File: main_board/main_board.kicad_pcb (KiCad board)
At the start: 4 copper layers, 45 x 85 mm, 68 parts, among them J1 CON-SMA-EDGE-S, J2 TSW-104-14-F-S, J3 TSW-104-14-F-S, U1 LT1722CS5-TRMPBF, U12 MIC5365-3.3YC5-TR, U2 TS5A4624DCKR, U3 AD5160, U4 TS5A4624DCKR, U5 AD8031ARTZ-REEL7, U6 LT1722CS5-TRMPBF, U7 LTC2315CTS8-12-PBF, U8 LT1818IS5-TRMPBF, U9 AP63205WU-7

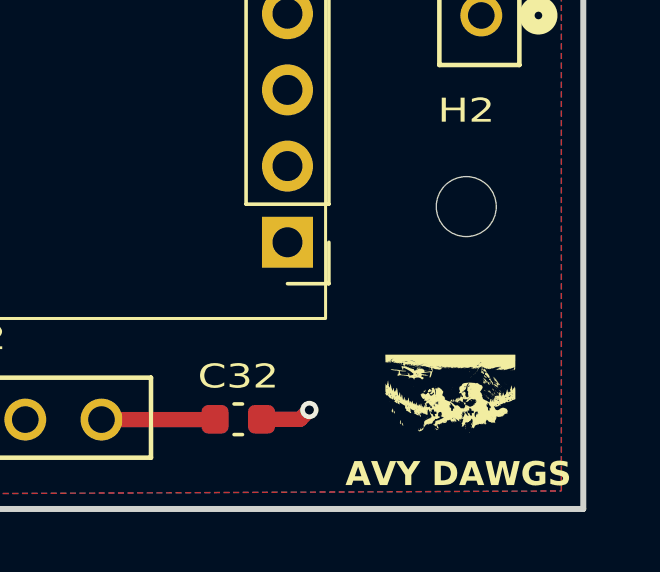
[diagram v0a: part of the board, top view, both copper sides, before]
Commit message: finalized main board, placing order from pcbway.
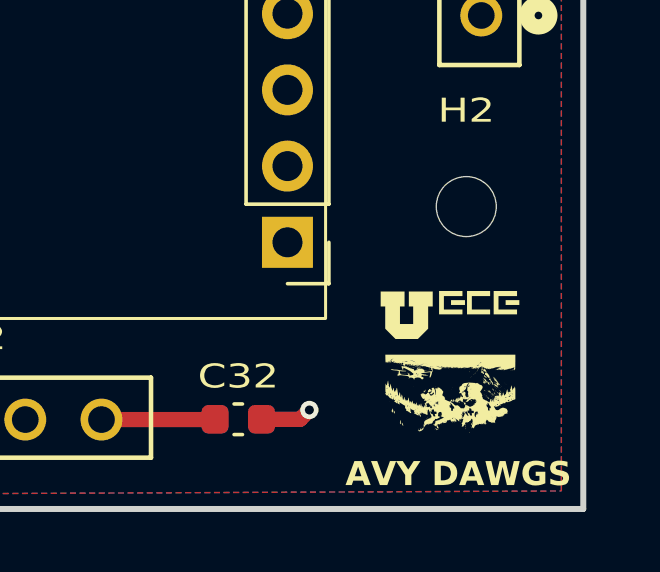
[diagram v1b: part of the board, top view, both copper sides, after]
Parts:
- added G***: LOGO, Graphics:uofu, F.Cu at (158.7, 145.8)
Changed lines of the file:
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@@
 		)
+	)
+	(footprint "Graphics:uofu"
+		(layer "F.Cu")
+		(at 158.7 145.8)
+		(property "Reference" "G***"
+			(at 0.012699 -2.5 0)
+			(layer "F.SilkS")
+			(hide yes)
+			(effects
+				(font
+					(size 1.5 1.5)
+					(thickness 0.3)
+				)
+			)
+		)
+		(property "Value" "LOGO"
+			(at 0.75 0 0)
+			(layer "F.SilkS")
+			(hide yes)
+			(effects
+				(font
+					(size 1.5 1.5)
+					(thickness 0.3)
+				)
+			)
+		)
+		(property "Datasheet" ""
+			(at 0 0 0)
+			(layer "F.Fab")
+			(hide yes)
+			(effects
+				(font
+					(size 1.27 1.27)
+					(thickness 0.15)
+				)
+			)
+		)
+		(property "Description" ""
+			(at 0 0 0)
+			(layer "F.Fab")
+			(hide yes)
+			(effects
+				(font
+					(size 1.27 1.27)
+					(thickness 0.15)
+				)
+			)
+		)
+		(attr board_only exclude_from_pos_files exclude_from_bom)
+		(fp_poly
+			(pts
+				(xy 0.486833 -0.381001) (xy 0.486833 -0.300567) (xy 0.253999 -0.300567) (xy 0.021166 -0.300567)
+				(xy 0.021166 -0.381001) (xy 0.021166 -0.461434) (xy 0.253999 -0.461434) (xy 0.486833 -0.461434)
+			)
+			(stroke
+				(width 0)
+				(type solid)
+			)
+			(fill yes)
+			(layer "F.SilkS")
+		)
+		(fp_poly
+			(pts
+				(xy 2.298699 -0.381001) (xy 2.298699 -0.300567) (xy 2.070099 -0.300567) (xy 1.841499 -0.300567)
+				(xy 1.841499 -0.381001) (xy 1.841499 -0.461434) (xy 2.070099 -0.461434) (xy 2.298699 -0.461434)
+			)
+			(stroke
+				(width 0)
+				(type solid)
+			)
+			(fill yes)
+			(layer "F.SilkS")
+		)
+		(fp_poly
+			(pts
+				(xy 0.402166 -0.681567) (xy 0.402166 -0.596901) (xy 0.093133 -0.596901) (xy -0.215901 -0.596901)
+				(xy -0.215901 -0.372534) (xy -0.215901 -0.148168) (xy 0.093133 -0.148168) (xy 0.402166 -0.148168)
+				(xy 0.402166 -0.067734) (xy 0.402166 0.012699) (xy 0.012699 0.012699) (xy -0.376767 0.012699) (xy -0.376767 -0.376767)
+				(xy -0.376767 -0.766234) (xy 0.012699 -0.766234) (xy 0.402166 -0.766234)
+			)
+			(stroke
+				(width 0)
+				(type solid)
+			)
+			(fill yes)
+			(layer "F.SilkS")
+		)
+		(fp_poly
+			(pts
+				(xy 1.325032 -0.681567) (xy 1.325032 -0.596901) (xy 1.020232 -0.596901) (xy 0.715433 -0.596901)
+				(xy 0.715433 -0.372534) (xy 0.715433 -0.148168) (xy 1.020232 -0.148168) (xy 1.325032 -0.148168)
+				(xy 1.325032 -0.067734) (xy 1.325032 0.012699) (xy 0.939799 0.012699) (xy 0.554566 0.012699) (xy 0.554566 -0.376767)
+				(xy 0.554566 -0.766234) (xy 0.939799 -0.766234) (xy 1.325032 -0.766234)
+			)
+			(stroke
+				(width 0)
+				(type solid)
+			)
+			(fill yes)
+			(layer "F.SilkS")
+		)
+		(fp_poly
+			(pts
+				(xy 2.222499 -0.681567) (xy 2.222499 -0.596901) (xy 1.913466 -0.596901) (xy 1.604432 -0.596901)
+				(xy 1.604432 -0.372534) (xy 1.604432 -0.148168) (xy 1.913466 -0.148168) (xy 2.222499 -0.148168)
+				(xy 2.222499 -0.067734) (xy 2.222499 0.012699) (xy 1.833033 0.012699) (xy 1.443566 0.012699) (xy 1.443566 -0.376767)
+				(xy 1.443566 -0.766234) (xy 1.833033 -0.766234) (xy 2.222499 -0.766234)
+			)
+			(stroke
+				(width 0)
+				(type solid)
+			)
+			(fill yes)
+			(layer "F.SilkS")
+		)
+		(fp_poly
+			(pts
+				(xy -1.528234 -0.499534) (xy -1.528234 -0.249767) (xy -1.604434 -0.249767) (xy -1.680634 -0.249767)
+				(xy -1.680634 0.042333) (xy -1.680634 0.334433) (xy -1.460501 0.334433) (xy -1.240367 0.334433)
+				(xy -1.240367 0.042333) (xy -1.240367 -0.249767) (xy -1.312334 -0.249767) (xy -1.384301 -0.249767)
+				(xy -1.384301 -0.499534) (xy -1.384301 -0.749301) (xy -0.986367 -0.749301) (xy -0.588434 -0.749301)
+				(xy -0.588434 -0.499534) (xy -0.588434 -0.249767) (xy -0.664634 -0.249767) (xy -0.740834 -0.249767)
+				(xy -0.740834 0.120727) (xy -0.740834 0.491221) (xy -0.91236 0.662593) (xy -1.083885 0.833966) (xy -1.456421 0.833966)
+				(xy -1.828956 0.833966) (xy -2.000328 0.66244) (xy -2.171701 0.490915) (xy -2.171701 0.120574) (xy -2.171701 -0.249767)
+				(xy -2.247901 -0.249767) (xy -2.324101 -0.249767) (xy -2.324101 -0.499534) (xy -2.324101 -0.749301)
+				(xy -1.926167 -0.749301) (xy -1.528234 -0.749301)
+			)
+			(stroke
+				(width 0)
+				(type solid)
+			)
+			(fill yes)
+			(layer "F.SilkS")
+		)
+		(embedded_fonts no)
 	)
 	(footprint "LT172x:S_5_ADI"

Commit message: main board gerbers and antenna board layout.
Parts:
- added J4: TSW-104-14-F-S, pin_header_fp:CON4_1X4_TU_TSW, F.Cu at (159.7, 109.7)

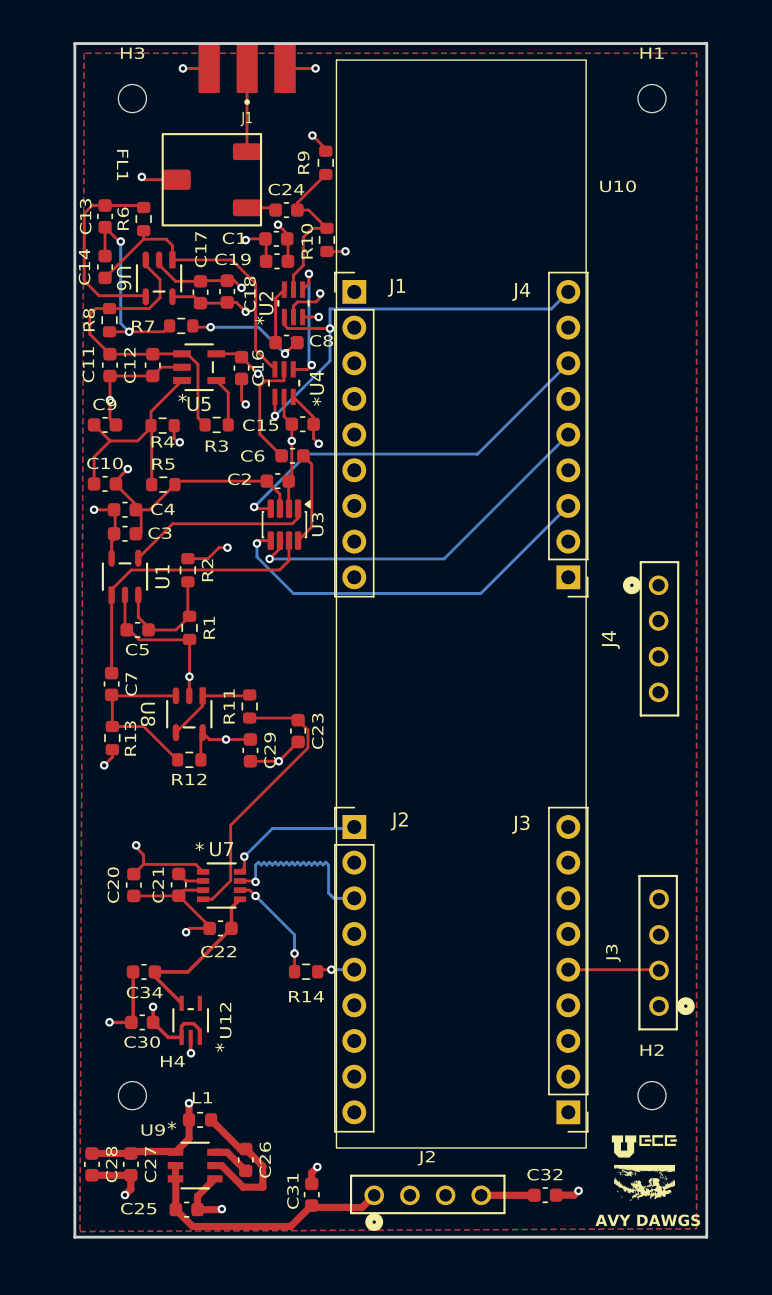
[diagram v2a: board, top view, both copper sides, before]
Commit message: Fixed edge clearance for both boards, both DRC clean
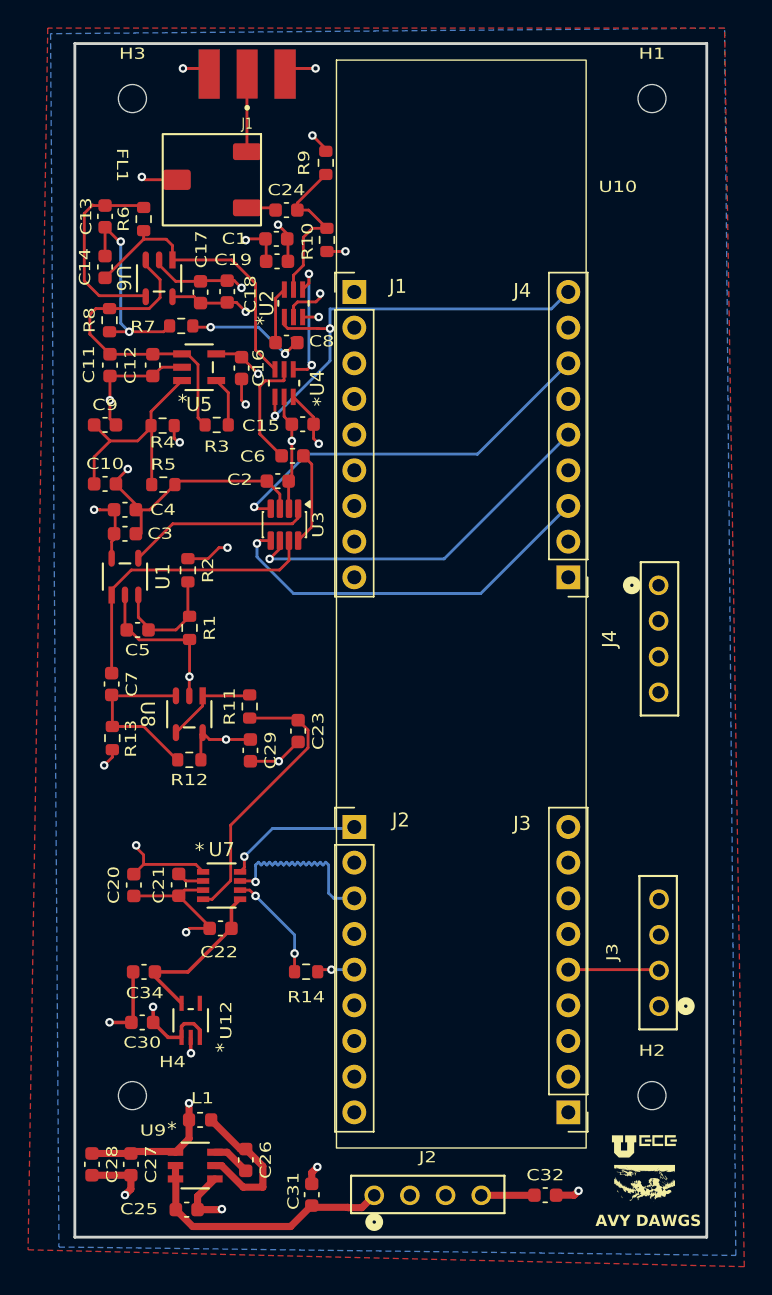
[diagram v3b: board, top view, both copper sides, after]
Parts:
- moved J1 0.40 mm to (130.4, 69.5)
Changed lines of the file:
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@@
 	(footprint "SMA_male_fp:RFSOLUTIONS_CON-SMA-EDGE-S"
 		(layer "F.Cu")
-		(at 130.4 69.0725 -90)
+		(at 130.4 69.4725 -90)
 		(property "Reference" "J1"
-			(at 3.5275 0 180)
+			(at 3.5275 0 0)
 			(layer "F.SilkS")
 			(effects
@@
 		(polygon
 			(pts
-				(xy 118.8 68) (xy 118.5 151.9) (xy 162.4 151.7) (xy 162.4 68)
+				(xy 116.2 66.2) (xy 114.8 153.2) (xy 165.8 154.4) (xy 164.4 66.2)
 			)
 		)
@@
 		(polygon
 			(pts
-				(xy 118.5 151.9) (xy 162.4 151.7) (xy 162.4 68) (xy 118.8 68)
+				(xy 117 153) (xy 165.2 153.6) (xy 164.4 66.2) (xy 116.4 66.6)
 			)
 		)
@@
 		(polygon
 			(pts
-				(xy 118.8 68) (xy 118.5 151.9) (xy 162.4 151.7) (xy 162.4 68)
+				(xy 116.4 66.4) (xy 116.8 153) (xy 165 153) (xy 164.4 66.2)
 			)
 		)
@@
 		(polygon
 			(pts
-				(xy 118.8 68) (xy 118.5 151.9) (xy 162.4 151.7) (xy 162.4 68)
+				(xy 116.6 66.4) (xy 116.4 153) (xy 165.4 154) (xy 164.4 66.2)
 			)
 		)
